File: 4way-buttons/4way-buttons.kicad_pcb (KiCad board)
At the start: 2 copper layers, 50 x 65.1 mm, 8 parts, among them J1 Conn_01x08_Male, J2 Conn_01x08_Male, SW1 SW_Push, SW2 SW_Push, SW3 SW_Push, SW4 SW_Push, SW5 SW_Push, SW6 SW_Push

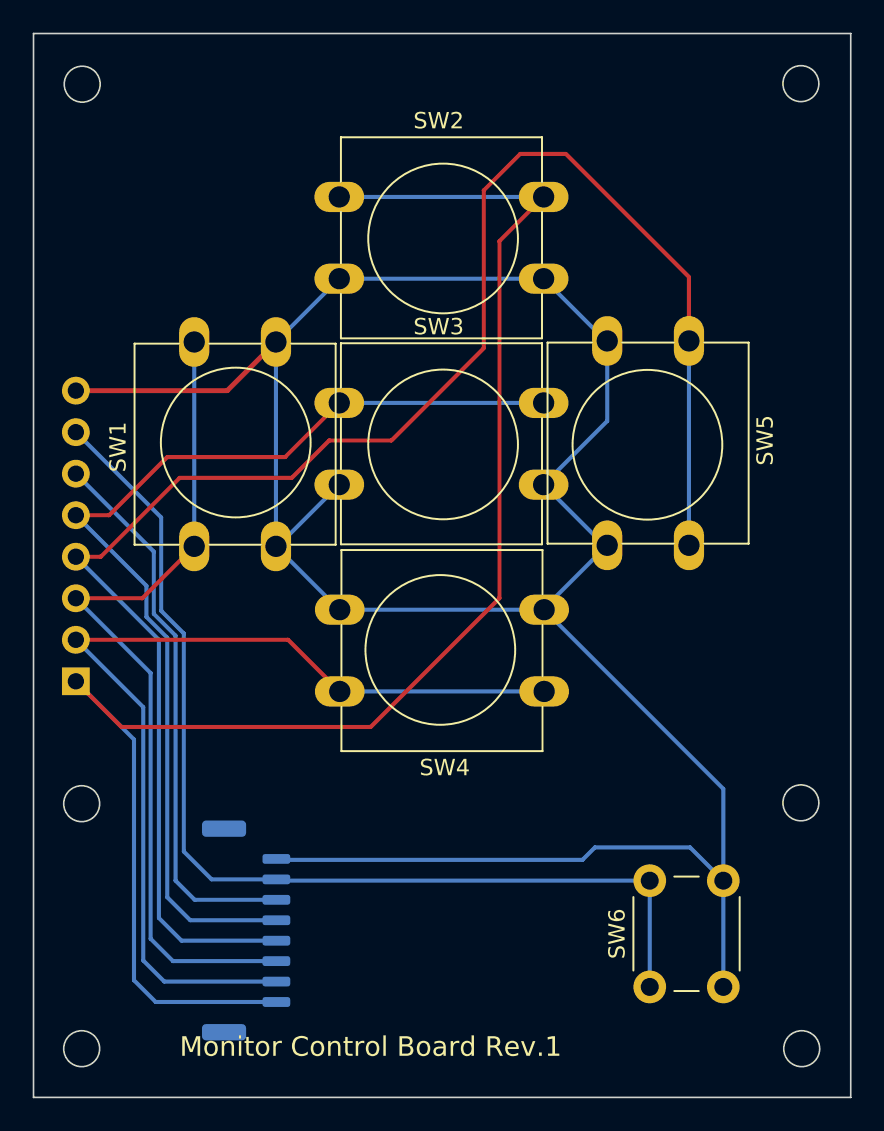
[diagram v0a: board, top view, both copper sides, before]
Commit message: 모니터 컨트를 버튼 보드 이미지 추가
Signed-off-by: Ju, Gyeong-min <jcmh74@gmail.com>
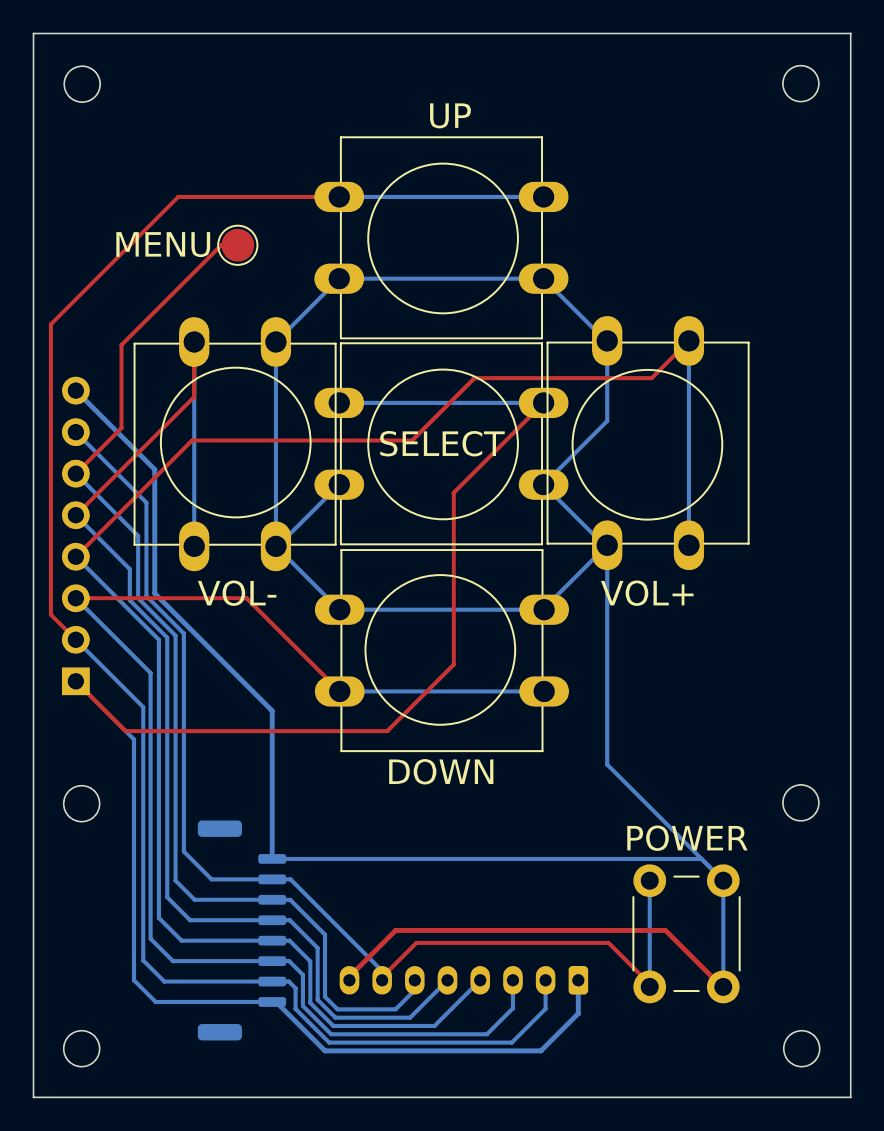
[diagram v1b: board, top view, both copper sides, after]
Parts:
- added J3: Conn_01x08_Male, Connector_JST:JST_PH_S8B-PH-K_1x08_P2.00mm_Horizontal, B.Cu at (162.1, 115.6)
- added TP1: TestPoint, TestPoint:TestPoint_Pad_D2.0mm, F.Cu at (141.2, 70.6)
- moved J1 0.25 mm to (141.5, 112.5)
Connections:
- net /RIGHT renamed /VOL_P
- J1 pad 1: /UP -> /SELECT
- J1 pad 2: /DOWN -> /UP
- J1 pad 3: /LEFT -> /DOWN
- J1 pad 5: /CENTER -> /VOL_M
- J2 pad 1: /UP -> /SELECT
- J2 pad 2: /DOWN -> /UP
- J2 pad 3: /LEFT -> /DOWN
- J2 pad 5: /CENTER -> /VOL_M
- SW1 pad 1: /LEFT -> /VOL_M
- SW3 pad 1: /CENTER -> /SELECT
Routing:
- net /SELECT: track 0.00 -> 108.6 mm
- net /VOL_M: track 0.00 -> 74.8 mm
- net /CENTER: track 64.4 -> 0.00 mm
- net /LEFT: track 52.0 -> 0.00 mm
- net GND: track 150.4 -> 198.2 mm
- net /MENU: track 34.1 -> 67.3 mm
- net /DOWN: track 60.0 -> 81.8 mm
- net /UP: track 97.5 -> 104.7 mm
- net /POWER: track 64.1 -> 69.3 mm
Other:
- board text added: "D"
- board text added: "DOWN"
- board text added: "G"
- board text added: "M"
- board text added: "MENU"
- board text added: "POWER"
- board text added: "PW"
- board text added: "SEL"
- board text added: "SELECT"
- board text added: "U"
- board text added: "UP"
- board text added: "V+"
- board text added: "V-"
- board text added: "VOL+"
- board text added: "VOL-"
